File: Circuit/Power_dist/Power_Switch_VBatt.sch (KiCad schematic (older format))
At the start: 8 parts, among them P5 XT60, Q2 IPD90P03P4L

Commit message: edit sch and add pcix16
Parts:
- F2: footprint Zeabus:FUSE_AUTO -> zeabus:FUSE_AUTO
- Q2: footprint TO_SOT_Packages_SMD:TO-252-2Lead -> TO_SOT_Packages_SMD:TO-252-2
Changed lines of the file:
@@
 EESchema Schematic File Version 2
+LIBS:Power_Distributor-rescue
 LIBS:power
 LIBS:device
@@
 LIBS:zeabus
 LIBS:ftdi
+LIBS:Power_Distributor-cache
 EELAYER 25 0
 EELAYER END
 $Descr A4 11693 8268
 encoding utf-8
-Sheet 3 9
+Sheet 4 9
 Title "DVL and Sonar Switch"
 Date "2017-04-06"
@@
 F 0 "Q3" H 6550 3350 50  0000 L CNN
 F 1 "IPD90P03P4L" H 6550 3250 50  0000 L CNN
-F 2 "TO_SOT_Packages_SMD:TO-252-2Lead" H 6550 3400 50  0001 C CNN
+F 2 "TO_SOT_Packages_SMD:TO-252-2" H 6550 3400 50  0001 C CNN
 F 3 "" H 6350 3300 50  0001 C CNN
 	1    6350 3300
@@
 $EndComp
 $Comp
-L GND #PWR012
+L GND #PWR021
 U 1 1 58E527F8
 P 6450 4950
-AR Path="/58E51F99/58E527F8" Ref="#PWR012"  Part="1"
-AR Path="/58E527AF/58E527F8" Ref="#PWR013"  Part="1"
-F 0 "#PWR013" H 6450 4700 50  0001 C CNN
+AR Path="/58E51F99/58E527F8" Ref="#PWR021"  Part="1"
+AR Path="/58E527AF/58E527F8" Ref="#PWR022"  Part="1"
+F 0 "#PWR022" H 6450 4700 50  0001 C CNN
 F 1 "GND" H 6450 4800 50  0000 C CNN
 F 2 "" H 6450 4950 50  0001 C CNN
@@
 F 0 "F3" V 6530 3750 50  0000 C CNN
 F 1 "Fuse" V 6375 3750 50  0000 C CNN
-F 2 "Zeabus:FUSE_AUTO" V 6380 3750 50  0001 C CNN
+F 2 "zeabus:FUSE_AUTO" V 6380 3750 50  0001 C CNN
 F 3 "" H 6450 3750 50  0001 C CNN
 	1    6450 3750

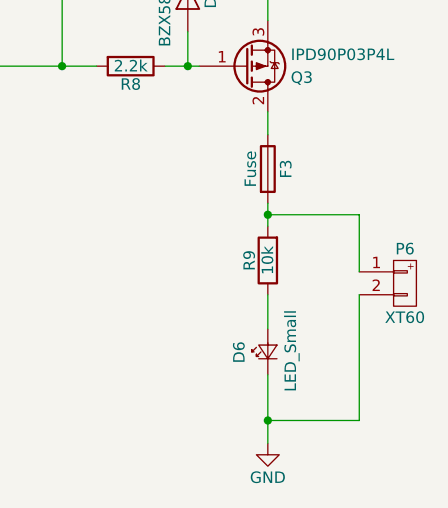
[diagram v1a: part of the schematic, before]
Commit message: delete fuses at thrusters and oring + add power on jumper
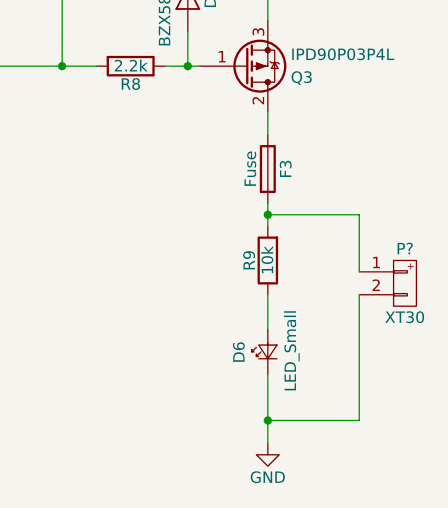
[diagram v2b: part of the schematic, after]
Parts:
- removed P5: XT60, zeabus:XT60, symbol XT60
- added P?: XT30, symbol XT30
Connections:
- net GND: now also P?.2 (P2)
- net at F2.2, R6.2: now also P?.1 (P1)
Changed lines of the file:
@@
 $Descr A4 11693 8268
 encoding utf-8
-Sheet 4 9
+Sheet 4 8
 Title "DVL and Sonar Switch"
 Date "2017-04-06"
@@
 	1    5850 3300
 	0    1    1    0
-$EndComp
-$Comp
-L XT60 P5
-U 1 1 58E521F9
-P 7050 4250
-AR Path="/58E51F99/58E521F9" Ref="P5"  Part="1"
-AR Path="/58E527AF/58E521F9" Ref="P6"  Part="1"
-F 0 "P6" H 7050 4400 50  0000 C CNN
-F 1 "XT60" H 7050 4100 50  0000 C CNN
-F 2 "zeabus:XT60" H 7150 4000 60  0001 C CNN
-F 3 "" H 7050 4250 60  0000 C CNN
-	1    7050 4250
-	1    0    0    -1
 $EndComp
 $Comp
@@
 Wire Wire Line
 	6850 4850 6450 4850
+$Comp
+L XT30 P?
+U 1 1 5A39572B
+P 7050 4250
+AR Path="/58E51F99/5A39572B" Ref="P?"  Part="1"
+AR Path="/58E527AF/5A39572B" Ref="P?"  Part="1"
+F 0 "P?" H 7050 4400 50  0000 C CNN
+F 1 "XT30" H 7050 4100 50  0000 C CNN
+F 2 "" H 7050 4250 60  0000 C CNN
+F 3 "" H 7050 4250 60  0000 C CNN
+	1    7050 4250
+	1    0    0    -1
+$EndComp
 $EndSCHEMATC

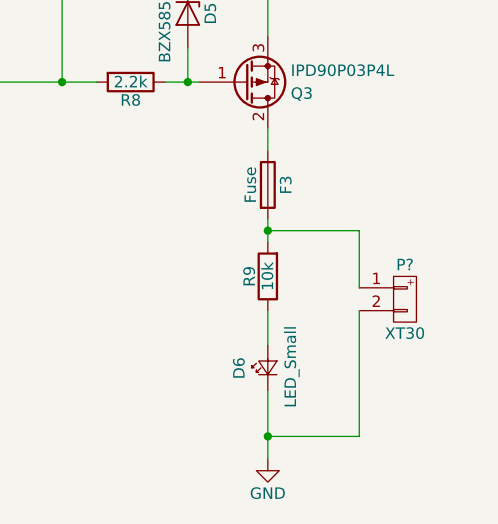
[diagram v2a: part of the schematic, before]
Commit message: component alignment on pcb
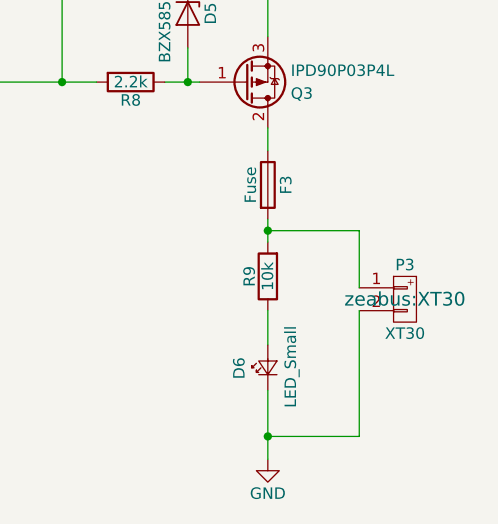
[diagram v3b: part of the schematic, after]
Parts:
- D4: footprint LEDs:LED_0603 -> LEDs:LED_0603_HandSoldering
- P2: renamed from P?; footprint (none) -> zeabus:XT30
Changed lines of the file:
@@
 F 0 "D6" H 6400 4675 50  0000 L CNN
 F 1 "LED_Small" H 6275 4450 50  0000 L CNN
-F 2 "LEDs:LED_0603" V 6450 4550 50  0001 C CNN
+F 2 "LEDs:LED_0603_HandSoldering" V 6450 4550 50  0001 C CNN
 F 3 "" V 6450 4550 50  0001 C CNN
 	1    6450 4550
@@
 $EndComp
 $Comp
-L GND #PWR021
+L GND #PWR027
 U 1 1 58E527F8
 P 6450 4950
-AR Path="/58E51F99/58E527F8" Ref="#PWR021"  Part="1"
-AR Path="/58E527AF/58E527F8" Ref="#PWR022"  Part="1"
-F 0 "#PWR022" H 6450 4700 50  0001 C CNN
+AR Path="/58E51F99/58E527F8" Ref="#PWR027"  Part="1"
+AR Path="/58E527AF/58E527F8" Ref="#PWR028"  Part="1"
+F 0 "#PWR028" H 6450 4700 50  0001 C CNN
 F 1 "GND" H 6450 4800 50  0000 C CNN
 F 2 "" H 6450 4950 50  0001 C CNN
@@
 	6850 4850 6450 4850
 $Comp
-L XT30 P?
+L XT30 P2
 U 1 1 5A39572B
 P 7050 4250
-AR Path="/58E51F99/5A39572B" Ref="P?"  Part="1"
-AR Path="/58E527AF/5A39572B" Ref="P?"  Part="1"
-F 0 "P?" H 7050 4400 50  0000 C CNN
+AR Path="/58E51F99/5A39572B" Ref="P2"  Part="1"
+AR Path="/58E527AF/5A39572B" Ref="P3"  Part="1"
+F 0 "P3" H 7050 4400 50  0000 C CNN
 F 1 "XT30" H 7050 4100 50  0000 C CNN
-F 2 "" H 7050 4250 60  0000 C CNN
+F 2 "zeabus:XT30" H 7050 4250 60  0000 C CNN
 F 3 "" H 7050 4250 60  0000 C CNN
 	1    7050 4250
